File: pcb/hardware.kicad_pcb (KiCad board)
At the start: 2 copper layers, 150 parts, among them J1 Micro_SD_Card_Det_Hirose_DM3AT, U1 AS4C512M16D3L-12BIN, U2 A33, U3 TPS62095RGTR, U4 TPS62095RGTR, U5 TPS62095RGTR, U6 TPS62095RGTR, U7 AP131-25

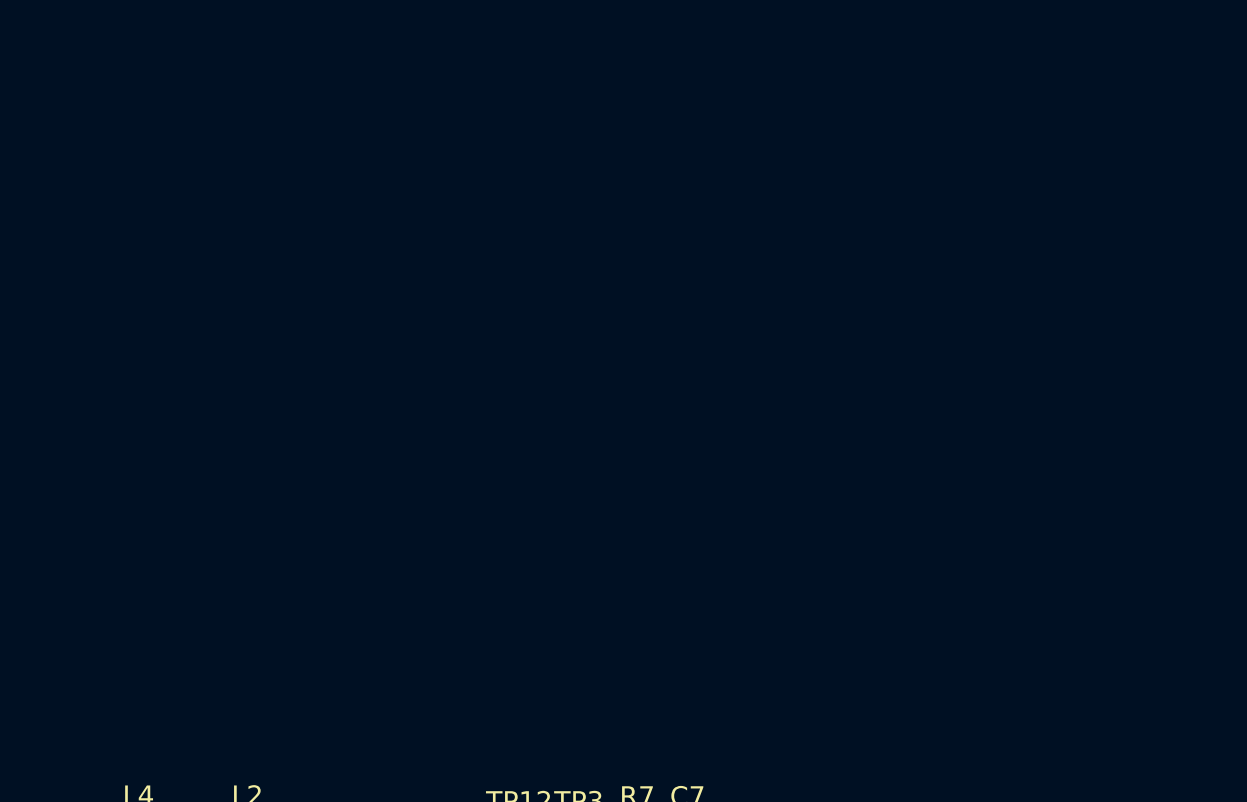
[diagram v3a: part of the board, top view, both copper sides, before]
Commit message: Added in the mains to 5V module, this will most likely be removed in the future.
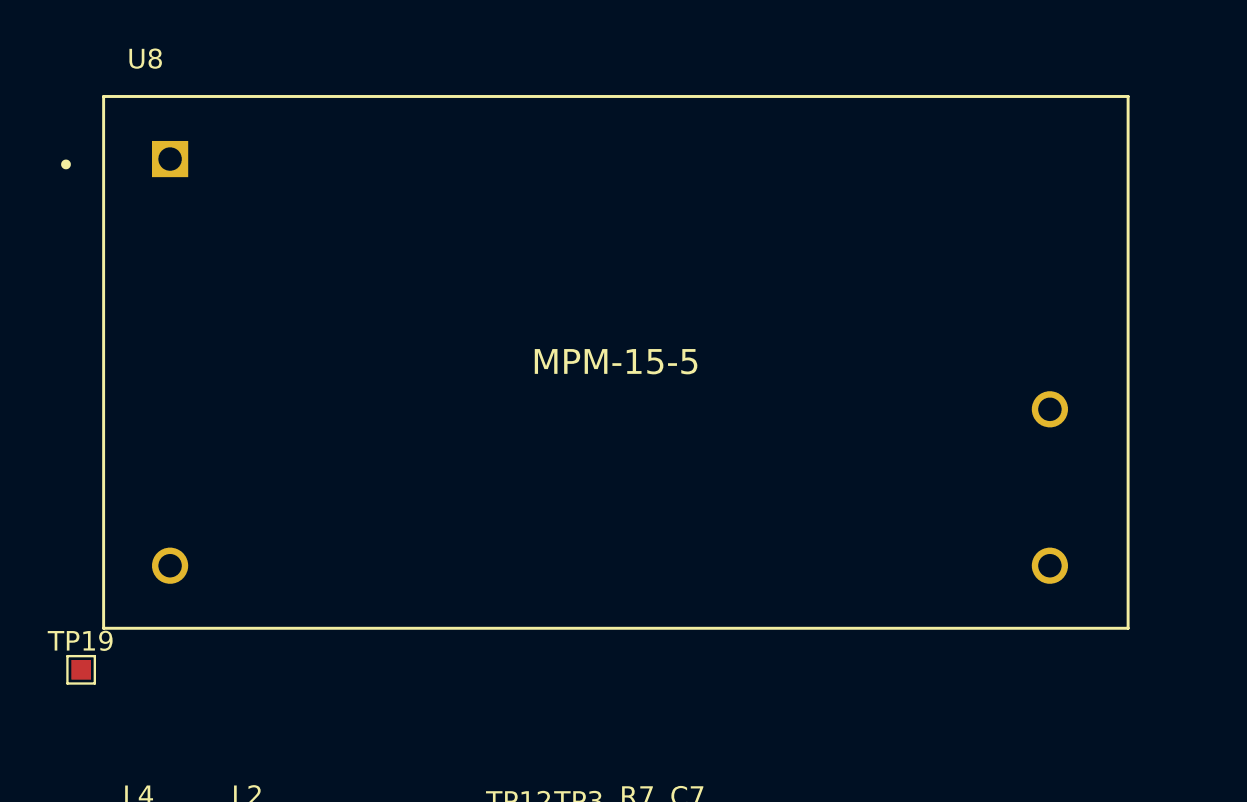
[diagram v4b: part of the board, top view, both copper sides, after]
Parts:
- added TP19: TestPoint, TestPoint:TestPoint_Pad_1.0x1.0mm, F.Cu at (69.8, 59.7)
- added U8: MPM-15-5, MPM-15-5:MEAN_WELL-MPM-15-5-MFG, F.Cu at (97.2, 44.0)
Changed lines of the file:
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@@
     (tracks 0)
     (zones 0)
-    (modules 150)
-    (nets 253)
+    (modules 152)
+    (nets 255)
   )
   (page A4)
@@
   (net 251 /HPVCCBP)
   (net 252 /VCC-EFUSE)
+  (net 253 /a33_power/AC_N)
+  (net 254 /a33_power/AC_L)
   (net_class Default "This is the default net class."
     (clearance 0.2)
@@
     (add_net /HPVCCBP)
     (add_net /VCC-EFUSE)
+    (add_net /a33_power/AC_L)
+    (add_net /a33_power/AC_N)
     (add_net /gpio/SD_CLK)
     (add_net /gpio/SD_CMD)
@@
     (add_net dba2)
   )
+  (module MPM-15-5:MEAN_WELL-MPM-15-5-MFG (layer F.Cu)
+    (at 97.2 43.965)
+    (fp_text reference U8 (at -25 -15.5) (layer F.SilkS)
+      (effects (font (size 1 1) (thickness 0.15)) (justify left))
+    )
+    (fp_text value MPM-15-5 (at 0 0) (layer F.SilkS)
+      (effects (font (size 1.27 1.27) (thickness 0.15)))
+    )
+    (fp_line (start -26.2 13.6) (end -26.2 -13.6) (layer F.Fab) (width 0.15))
+    (fp_line (start -26.2 -13.6) (end 26.2 -13.6) (layer F.Fab) (width 0.15))
+    (fp_line (start 26.2 -13.6) (end 26.2 13.6) (layer F.Fab) (width 0.15))
+    (fp_line (start 26.2 13.6) (end -26.2 13.6) (layer F.Fab) (width 0.15))
+    (fp_line (start -26.2 13.6) (end -26.2 -13.6) (layer F.SilkS) (width 0.15))
+    (fp_line (start -26.2 -13.6) (end 26.2 -13.6) (layer F.SilkS) (width 0.15))
+    (fp_line (start 26.2 -13.6) (end 26.2 13.6) (layer F.SilkS) (width 0.15))
+    (fp_line (start 26.2 13.6) (end -26.2 13.6) (layer F.SilkS) (width 0.15))
+    (fp_circle (center -28.125 -10.125) (end -28 -10.125) (layer F.SilkS) (width 0.25))
+    (fp_line (start 26.225 -13.625) (end 26.225 -13.625) (layer F.CrtYd) (width 0.15))
+    (fp_line (start 26.225 -13.625) (end -26.225 -13.625) (layer F.CrtYd) (width 0.15))
+    (fp_line (start -26.225 -13.625) (end -26.225 13.625) (layer F.CrtYd) (width 0.15))
+    (fp_line (start -26.225 13.625) (end 26.225 13.625) (layer F.CrtYd) (width 0.15))
+    (fp_line (start 26.225 13.625) (end 26.225 -13.625) (layer F.CrtYd) (width 0.15))
+    (pad 4 thru_hole circle (at 22.2 10.4) (size 1.85 1.85) (drill 1.2) (layers *.Cu)
+      (net 185 GND))
+    (pad 3 thru_hole circle (at -22.8 10.4) (size 1.85 1.85) (drill 1.2) (layers *.Cu)
+      (net 253 /a33_power/AC_N))
+    (pad 2 thru_hole circle (at 22.2 2.4) (size 1.85 1.85) (drill 1.2) (layers *.Cu)
+      (net 213 +5V))
+    (pad 1 thru_hole rect (at -22.8 -10.4) (size 1.85 1.85) (drill 1.2) (layers *.Cu)
+      (net 254 /a33_power/AC_L))
+    (model eec.models/MEAN_WELL_-_MPM-15-5.step
+      (at (xyz 0 0 0))
+      (scale (xyz 1 1 1))
+      (rotate (xyz 0 0 0))
+    )
+  )
+  (module TestPoint:TestPoint_Pad_1.0x1.0mm (layer F.Cu)
+    (at 69.85 59.69)
+    (descr "SMD rectangular pad as test Point, square 1.0mm side length")
+    (tags "test point SMD pad rectangle square")
+    (attr virtual)
+    (fp_text reference TP19 (at 0 -1.448) (layer F.SilkS)
+      (effects (font (size 1 1) (thickness 0.15)))
+    )
+    (fp_text value TestPoint (at 0 1.55) (layer F.Fab)
+      (effects (font (size 1 1) (thickness 0.15)))
+    )
+    (fp_text user %R (at 0 -1.45) (layer F.Fab)
+      (effects (font (size 1 1) (thickness 0.15)))
+    )
+    (fp_line (start -0.7 -0.7) (end 0.7 -0.7) (layer F.SilkS) (width 0.12))
+    (fp_line (start 0.7 -0.7) (end 0.7 0.7) (layer F.SilkS) (width 0.12))
+    (fp_line (start 0.7 0.7) (end -0.7 0.7) (layer F.SilkS) (width 0.12))
+    (fp_line (start -0.7 0.7) (end -0.7 -0.7) (layer F.SilkS) (width 0.12))
+    (fp_line (start -1 -1) (end 1 -1) (layer F.CrtYd) (width 0.05))
+    (fp_line (start -1 -1) (end -1 1) (layer F.CrtYd) (width 0.05))
+    (fp_line (start 1 1) (end 1 -1) (layer F.CrtYd) (width 0.05))
+    (fp_line (start 1 1) (end -1 1) (layer F.CrtYd) (width 0.05))
+    (pad 1 smd rect (at 0 0) (size 1 1) (layers F.Cu F.Mask)
+      (net 213 +5V))
+  )
   (module AS4C512M16D3L:Alliance_Memory-AS4C512M16D3L-12BIN-0-0-IPC_A (layer F.Cu)

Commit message: Figured out all the crystals
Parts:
- added R27: 0R, Resistor_SMD:R_0402_1005Metric, F.Cu at (86.7, 37.6)
- added R28: 0R, Resistor_SMD:R_0402_1005Metric, F.Cu at (89.6, 37.6)
- added Y1: 24Mhz, Crystal:Crystal_SMD_Abracon_ABM8G-4Pin_3.2x2.5mm, F.Cu at (138.7, 113.8)
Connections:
- U2 pad G1: /ram/CK -> Net-(R27-Pad1)
- U2 pad G2: /ram/!CK -> Net-(R28-Pad1)

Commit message: Backing up
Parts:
- added C100: 100nF, Capacitor_SMD:C_0402_1005Metric, F.Cu at (144.2, 57.2)
- added C101: 1uF, Capacitor_SMD:C_0402_1005Metric, F.Cu at (153.2, 53.0)
- added C102: 10uF, Capacitor_SMD:C_0402_1005Metric, F.Cu at (146.5, 57.2)
- added C103: 10uF, Capacitor_SMD:C_0402_1005Metric, F.Cu at (148.7, 55.6)
- added C104: 100nF, Capacitor_SMD:C_0402_1005Metric, F.Cu at (153.2, 54.6)
- added C105: 10uF, Capacitor_SMD:C_0402_1005Metric, F.Cu at (200.7, 63.5)
- added C106: 10uF, Capacitor_SMD:C_0402_1005Metric, F.Cu at (200.7, 65.2)
- added C95: 10pF, Capacitor_SMD:C_0402_1005Metric, F.Cu at (137.5, 57.6)
- added C96: 10pF, Capacitor_SMD:C_0402_1005Metric, F.Cu at (139.7, 57.6)
- added C97: 30pF, Capacitor_SMD:C_0402_1005Metric, F.Cu at (142.0, 57.6)
- added C98: 30pF, Capacitor_SMD:C_0402_1005Metric, F.Cu at (144.2, 55.6)
- added C99: 10uF, Capacitor_SMD:C_0402_1005Metric, F.Cu at (146.5, 55.6)
- added J2: USB_A, Connector_USB:USB_A_Molex_105057_Vertical, F.Cu at (187.5, 69.4)
- added J3: USB_A, Connector_USB:USB_A_Molex_105057_Vertical, F.Cu at (187.5, 78.2)
- added R29: 10M, Resistor_SMD:R_0402_1005Metric, F.Cu at (153.6, 49.2)
- added R30: 10k, Resistor_SMD:R_0402_1005Metric, F.Cu at (137.8, 55.8)
- added R31: 10M, Resistor_SMD:R_0402_1005Metric, F.Cu at (153.6, 51.2)
- added R32: 200k, Resistor_SMD:R_0402_1005Metric, F.Cu at (140.7, 55.8)
- added Y2: 32.768khz, Abracon:Abracon-ABS05-0-0-MFG, F.Cu at (134.9, 56.2)
- C1, C10, C11, C12, C13, C14, C15, C16, C17, C18, C19, C2, C20, C21, C22, C23, C24, C25, C26, C27, C28, C29, C3, C30, C31, C32, C33, C34, C35, C36, C37, C38, C39, C4, C40, C41, C42, C43, C44, C45, C46, C47, C48, C49, C5, C50, C51, C52, C53, C54, C55, C56, C57, C58, C59, C6, C60, C61, C62, C63, C64, C65, C66, C67, C68, C69, C7, C70, C71, C72, C73, C74, C75, C76, C77, C78, C79, C8, C80, C81, C82, C83, C84, C85, C86, C87, C88, C89, C9, C90, C91, C92, C93, C94: footprint Capacitor_SMD:C_01005_0402Metric -> Capacitor_SMD:C_0402_1005Metric
- R27, R28: moved to B.Cu
- moved C10 112.8 mm to (206.1, 94.1)
- moved C12 112.8 mm to (205.4, 96.3)
- moved C13 112.8 mm to (207.7, 97.4)
- moved C14 112.8 mm to (210.6, 94.4)
- moved C16 112.8 mm to (210.6, 92.7)
- moved C17 112.8 mm to (207.7, 95.8)
- moved C18 112.8 mm to (205.4, 97.9)
- moved C21 112.8 mm to (208.3, 94.1)
- moved C24 112.8 mm to (203.2, 97.9)
- moved C9 112.8 mm to (203.2, 96.3)
- moved R11 112.8 mm to (206.6, 90.3)
- moved R4 112.8 mm to (199.5, 111.6)
- moved R5 112.8 mm to (199.5, 113.6)
- moved R6 112.8 mm to (202.4, 111.6)
- moved R9 112.8 mm to (206.6, 88.3)
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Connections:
- net Net-(U2-PadG16) renamed /gpio/UART0_RX
- net Net-(U2-PadG17) renamed /gpio/UART0_TX
- U1 pad A2: d13 -> Net-(U1-PadA2)
- U1 pad A3: d15 -> Net-(U1-PadA3)
- U1 pad A7: d12 -> Net-(U1-PadA7)
- U1 pad B8: d14 -> Net-(U1-PadB8)
- U1 pad C2: d11 -> Net-(U1-PadC2)
- U1 pad C3: d9 -> Net-(U1-PadC3)
- U1 pad C8: d10 -> Net-(U1-PadC8)
- U1 pad D7: d8 -> Net-(U1-PadD7)
- U1 pad E3: d0 -> Net-(U1-PadE3)
- U1 pad F2: d2 -> Net-(U1-PadF2)
- U1 pad F7: d1 -> Net-(U1-PadF7)
- U1 pad F8: d3 -> Net-(U1-PadF8)
- U1 pad G2: d6 -> Net-(U1-PadG2)
- U1 pad H3: d4 -> Net-(U1-PadH3)
- U1 pad H7: d7 -> Net-(U1-PadH7)
- U1 pad H8: d5 -> Net-(U1-PadH8)
- U1 pad M7: /ram/adr15 -> adr15
- U2 pad T4: Net-(U2-PadT4) -> Net-(C98-Pad1)
- U2 pad U4: Net-(U2-PadU4) -> Net-(C97-Pad1)
- Y1 pad 1: Net-(Y1-Pad1) -> Net-(C98-Pad1)
- Y1 pad 3: Net-(Y1-Pad3) -> Net-(C97-Pad1)
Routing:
- net adr0: track 0.00 -> 8.95 mm, vias 0 -> 2
- net adr10: track 0.00 -> 8.25 mm
- net adr15: track 0.00 -> 8.19 mm, vias 0 -> 2
- net adr4: track 0.00 -> 7.21 mm
- net adr9: track 0.00 -> 7.12 mm, vias 0 -> 2
- net adr7: track 0.00 -> 6.49 mm, vias 0 -> 2
- net adr5: track 0.00 -> 6.32 mm
- net adr12: track 0.00 -> 5.77 mm
- net adr2: track 0.00 -> 5.70 mm
- net adr13: track 0.00 -> 5.31 mm, vias 0 -> 2
- net /ram/!RST: track 0.00 -> 5.29 mm, vias 0 -> 2
- net adr11: track 0.00 -> 4.85 mm
- net adr1: track 0.00 -> 4.72 mm
- net adr6: track 0.00 -> 4.07 mm
- net adr8: track 0.00 -> 2.91 mm
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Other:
- copper layers 2 -> 4
- net class Default: clearance 0.2 -> 0.15; trace_width 0.25 -> 0.15; via_dia 0.8 -> 0.4; via_drill 0.4 -> 0.2
- net class Outer_Small added: clearance 0.1, trace_width 0.1, via_dia 0.4, via_drill 0.2
- net class Power added: clearance 0.2, trace_width 1, via_dia 0.8, via_drill 0.6
- rule trace_clearance: 0.2 -> 0.15
- rule trace_min: 0.2 -> 0.09
- rule via_min_drill: 0.3 -> 0.2

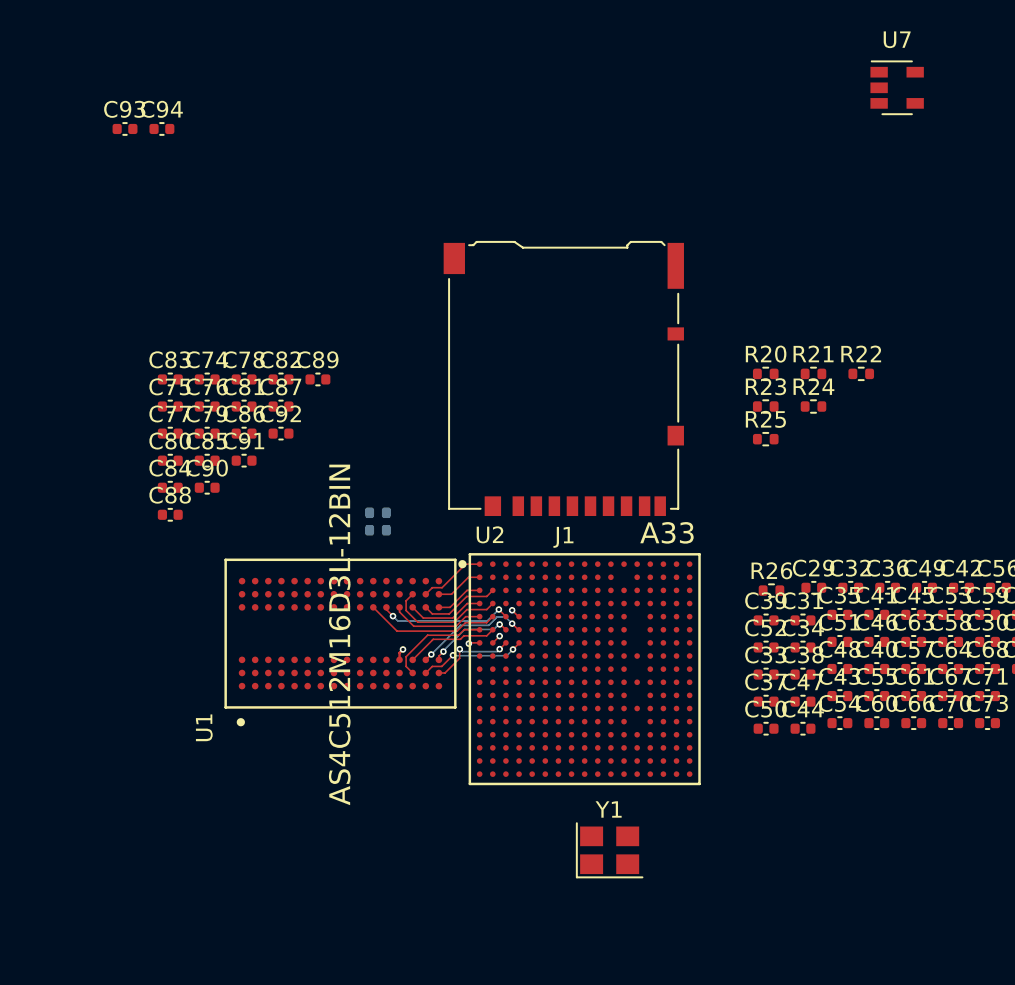
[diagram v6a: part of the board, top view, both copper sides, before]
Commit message: Repositioned the ram.
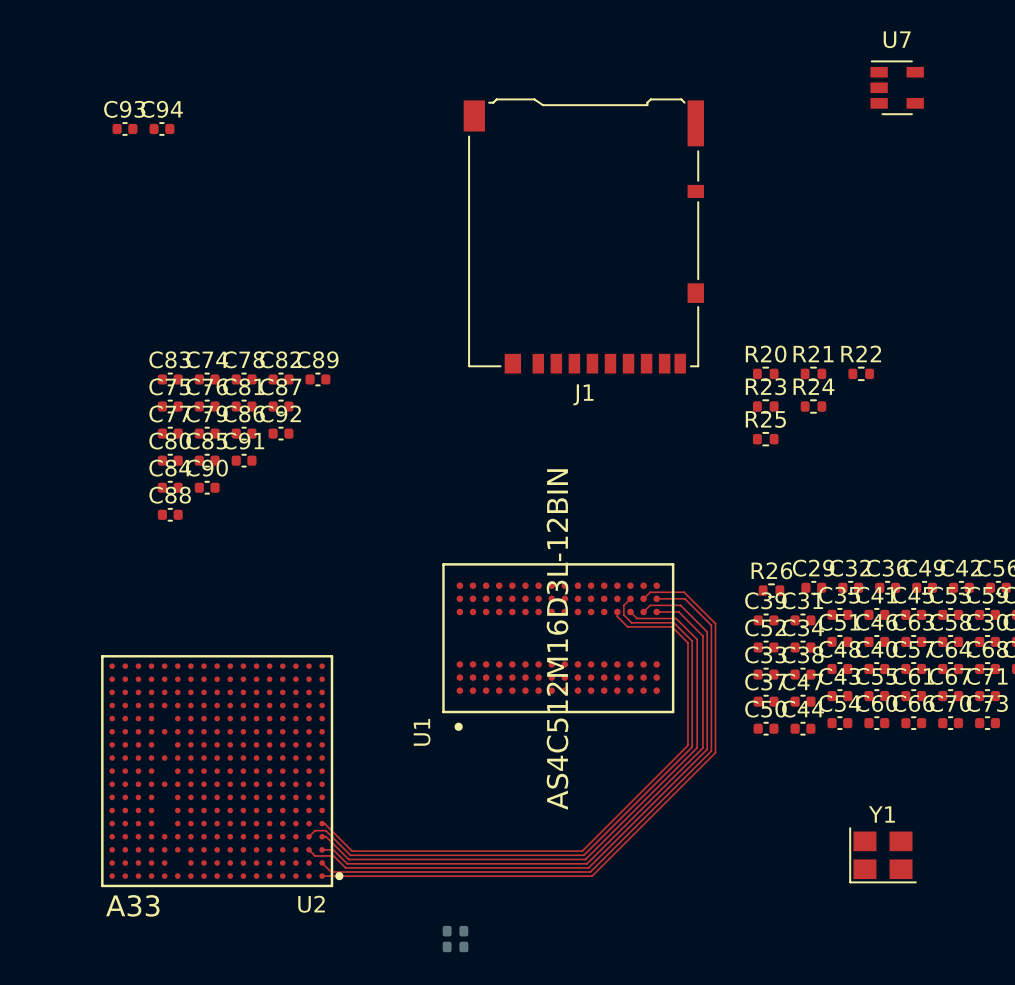
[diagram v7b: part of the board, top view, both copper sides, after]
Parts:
- R27, R28: value 0R -> 22R
- moved R28 25.9 mm to (129.3, 118.7)
- moved R27 25.8 mm to (129.3, 119.7)
- moved U2 23.3 mm to (114.8, 109.0), turned to 180 degrees
- moved Y1 16.7 mm to (155.3, 114.1)
- moved U1 13.3 mm to (135.6, 100.9)
- moved J1 8.77 mm to (137.1, 76.4)
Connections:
- U1 pad A1: +1V35 -> Net-(U1-PadA1)
- U1 pad A2: Net-(U1-PadA2) -> d13
- U1 pad A3: Net-(U1-PadA3) -> d15
- U1 pad A7: Net-(U1-PadA7) -> d12
- U1 pad A8: +1V35 -> Net-(U1-PadA8)
- U1 pad A9: GND -> Net-(U1-PadA9)
- U1 pad B1: GND -> Net-(U1-PadB1)
- U1 pad B2: +1V35 -> Net-(U1-PadB2)
- U1 pad B3: GND -> Net-(U1-PadB3)
- U1 pad B8: Net-(U1-PadB8) -> d14
- U1 pad B9: GND -> Net-(U1-PadB9)
- U1 pad C1: +1V35 -> Net-(U1-PadC1)
- U1 pad C2: Net-(U1-PadC2) -> d11
- U1 pad C3: Net-(U1-PadC3) -> d9
- U1 pad C8: Net-(U1-PadC8) -> d10
- U1 pad C9: +1V35 -> Net-(U1-PadC9)
- U1 pad D1: GND -> Net-(U1-PadD1)
- U1 pad D2: +1V35 -> Net-(U1-PadD2)
- U1 pad D7: Net-(U1-PadD7) -> d8
- U1 pad D8: GND -> Net-(U1-PadD8)
- U1 pad D9: +1V35 -> Net-(U1-PadD9)
- U1 pad E1: GND -> Net-(U1-PadE1)
- U1 pad E2: GND -> Net-(U1-PadE2)
- U1 pad E3: Net-(U1-PadE3) -> d0
- U1 pad E8: GND -> Net-(U1-PadE8)
- U1 pad E9: +1V35 -> Net-(U1-PadE9)
- U1 pad F1: +1V35 -> Net-(U1-PadF1)
- U1 pad F2: Net-(U1-PadF2) -> d2
- U1 pad F7: Net-(U1-PadF7) -> d1
- U1 pad F8: Net-(U1-PadF8) -> d3
- U1 pad F9: GND -> Net-(U1-PadF9)
- U1 pad G1: GND -> Net-(U1-PadG1)
- U1 pad G2: Net-(U1-PadG2) -> d6
- U1 pad G7: +1V35 -> Net-(U1-PadG7)
- U1 pad G8: GND -> Net-(U1-PadG8)
- U1 pad G9: GND -> Net-(U1-PadG9)
- U1 pad H2: +1V35 -> Net-(U1-PadH2)
- U1 pad H3: Net-(U1-PadH3) -> d4
- U1 pad H7: Net-(U1-PadH7) -> d7
- U1 pad H8: Net-(U1-PadH8) -> d5
- U1 pad H9: +1V35 -> Net-(U1-PadH9)
- U1 pad J2: GND -> Net-(U1-PadJ2)
- U1 pad J8: GND -> Net-(U1-PadJ8)
- U1 pad K2: +1V35 -> Net-(U1-PadK2)
- U1 pad K8: +1V35 -> Net-(U1-PadK8)
- U1 pad M1: GND -> Net-(U1-PadM1)
- U1 pad M9: GND -> Net-(U1-PadM9)
- U1 pad N1: +1V35 -> Net-(U1-PadN1)
- U1 pad N9: +1V35 -> Net-(U1-PadN9)
- U1 pad P1: GND -> Net-(U1-PadP1)
- U1 pad P9: GND -> Net-(U1-PadP9)
- U1 pad R1: +1V35 -> Net-(U1-PadR1)
- U1 pad R9: +1V35 -> Net-(U1-PadR9)
- U1 pad T1: GND -> Net-(U1-PadT1)
- U1 pad T9: GND -> Net-(U1-PadT9)
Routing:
- net adr6: track 4.07 -> 40.3 mm
- net adr8: track 2.91 -> 38.7 mm
- net adr11: track 4.85 -> 39.6 mm
- net adr14: track 2.91 -> 36.7 mm
- net adr1: track 4.72 -> 37.6 mm
- net adr4: track 7.21 -> 39.3 mm
- net adr12: track 5.77 -> 37.2 mm
- net adr0: track 8.95 -> 0.00 mm, vias 2 -> 0
- net adr10: track 8.25 -> 0.00 mm
- net adr15: track 8.19 -> 0.00 mm, vias 2 -> 0
- net adr9: track 7.12 -> 0.00 mm, vias 2 -> 0
- net adr7: track 6.49 -> 0.00 mm, vias 2 -> 0
- net adr5: track 6.32 -> 0.00 mm
- net adr2: track 5.70 -> 0.00 mm
- net adr13: track 5.31 -> 0.00 mm, vias 2 -> 0
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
